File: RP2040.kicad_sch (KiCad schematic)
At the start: 23 parts, among them U1 RP2040, Y1 12MHz

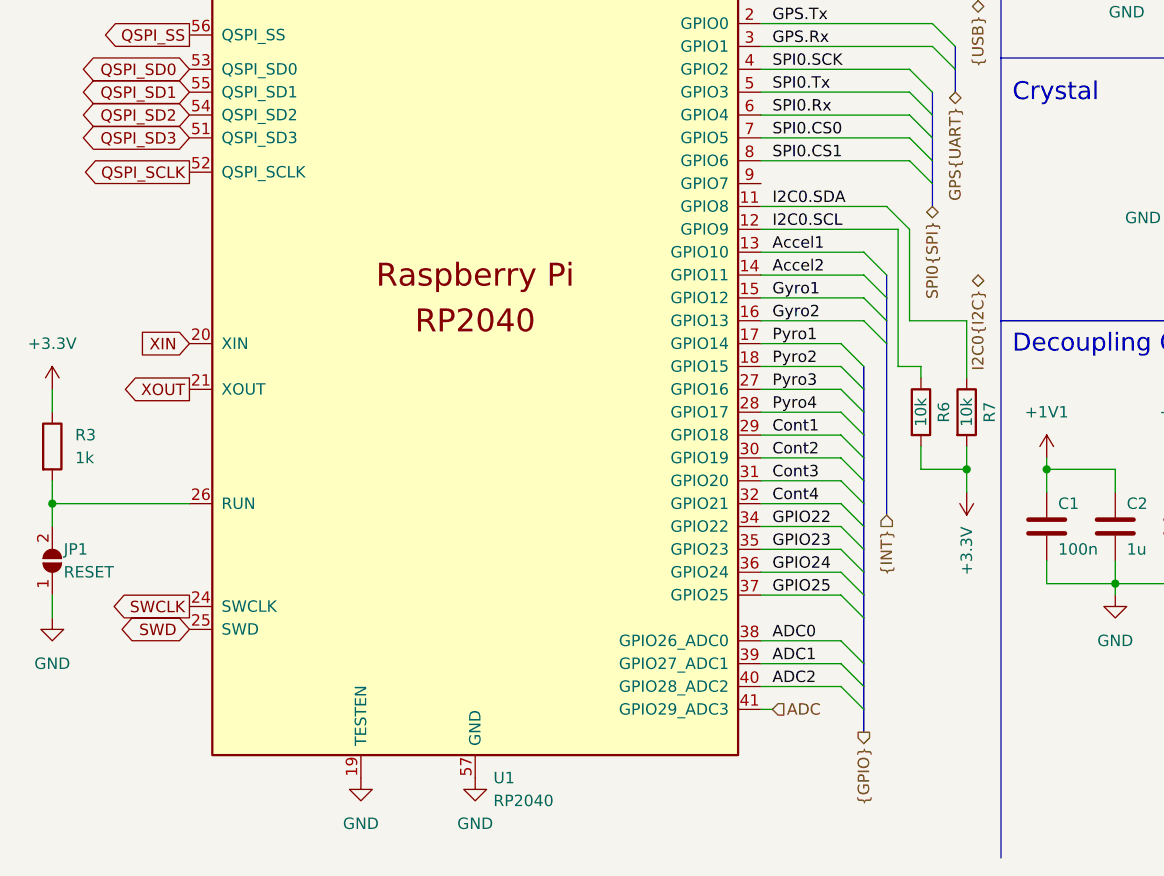
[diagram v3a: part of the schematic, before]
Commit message: Rearranged IO pins to make routing easier. Removed reset, changed BOOTSEL to button
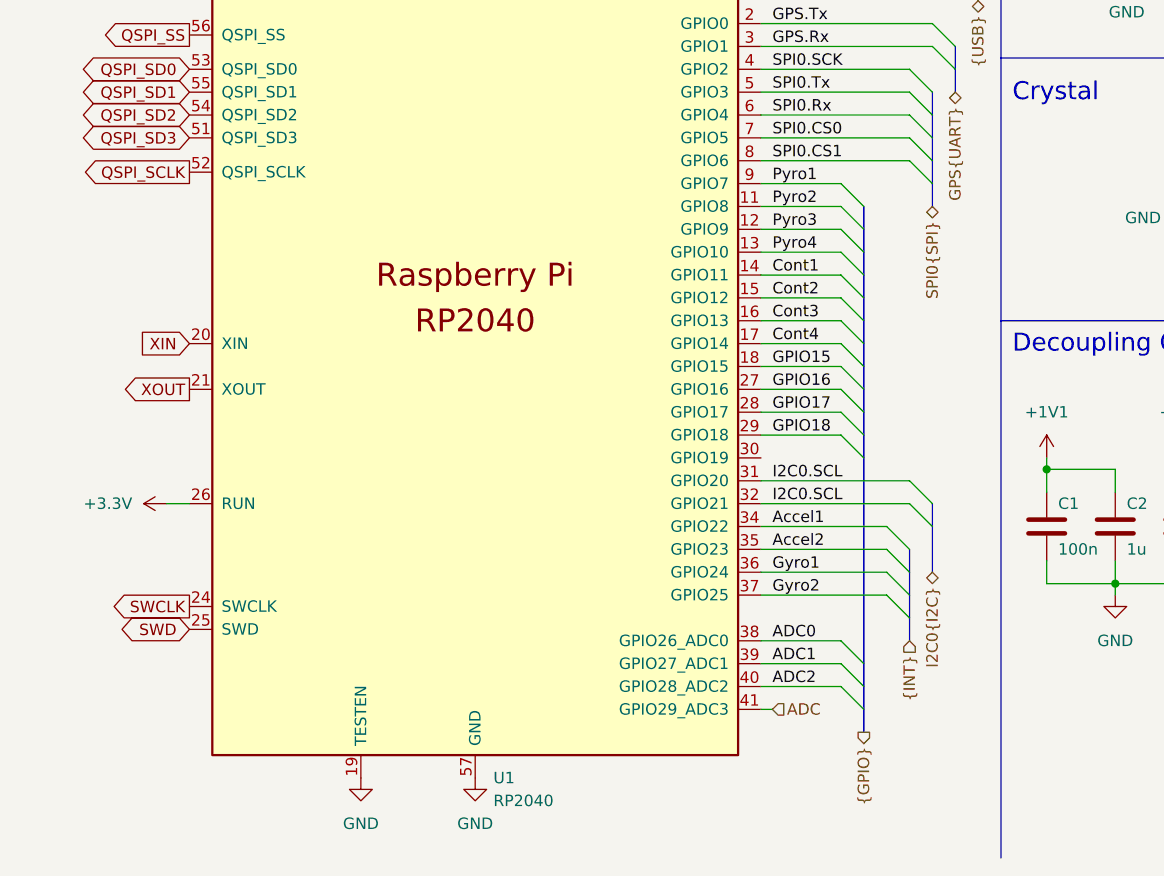
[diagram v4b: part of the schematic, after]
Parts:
- removed JP1: RESET, Jumper:SolderJumper-2_P1.3mm_Open_RoundedPad1.0x1.5mm, symbol Jumper:SolderJumper_2_Open
- removed R3: 1k, Resistor_SMD:R_0603_1608Metric, symbol Device:R
- removed R6, R7: 10k, Resistor_SMD:R_0603_1608Metric, symbol Device:R
- JP2: footprint Jumper:SolderJumper-2_P1.3mm_Open_RoundedPad1.0x1.5mm -> Button_Switch_SMD:SW_SPST_B3U-1000P
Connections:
- net GPIO22 is gone; now on net Accel1: U1.34 (GPIO22)
- net GPIO23 is gone; now on net Accel2: U1.35 (GPIO23)
- net GPIO24 is gone; now on net Gyro1: U1.36 (GPIO24)
- net GPIO25 is gone; now on net Gyro2: U1.37 (GPIO25)
- net I2C0.SDA is gone; now on net Pyro2: U1.11 (GPIO8)
- net +3V3: now also U1.26 (RUN)
- net Accel1: no longer U1.13 (GPIO10)
- net Accel2: no longer U1.14 (GPIO11)
- net Cont1: now also U1.14 (GPIO11); no longer U1.29 (GPIO18)
- net Cont2: now also U1.15 (GPIO12); no longer U1.30 (GPIO19)
- net Cont3: now also U1.16 (GPIO13); no longer U1.31 (GPIO20)
- net Cont4: now also U1.17 (GPIO14); no longer U1.32 (GPIO21)
- net Gyro1: no longer U1.15 (GPIO12)
- net Gyro2: no longer U1.16 (GPIO13)
- net I2C0.SCL: now also U1.31 (GPIO20), U1.32 (GPIO21); no longer U1.12 (GPIO9)
- net Pyro1: now also U1.9 (GPIO7); no longer U1.17 (GPIO14)
- net Pyro2: no longer U1.18 (GPIO15)
- net Pyro3: now also U1.12 (GPIO9); no longer U1.27 (GPIO16)
- net Pyro4: now also U1.13 (GPIO10); no longer U1.28 (GPIO17)
- new net GPIO15: U1.18 (GPIO15)
- new net GPIO16: U1.27 (GPIO16)
- new net GPIO17: U1.28 (GPIO17)
- new net GPIO18: U1.29 (GPIO18)

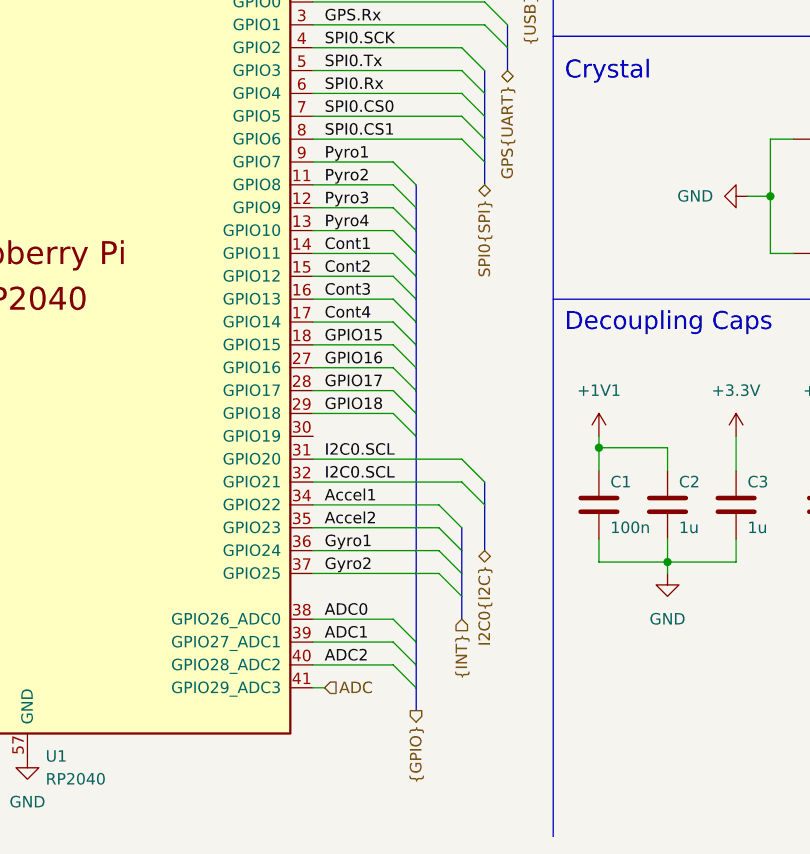
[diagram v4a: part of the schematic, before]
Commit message: Removed GPIO, changed footprints
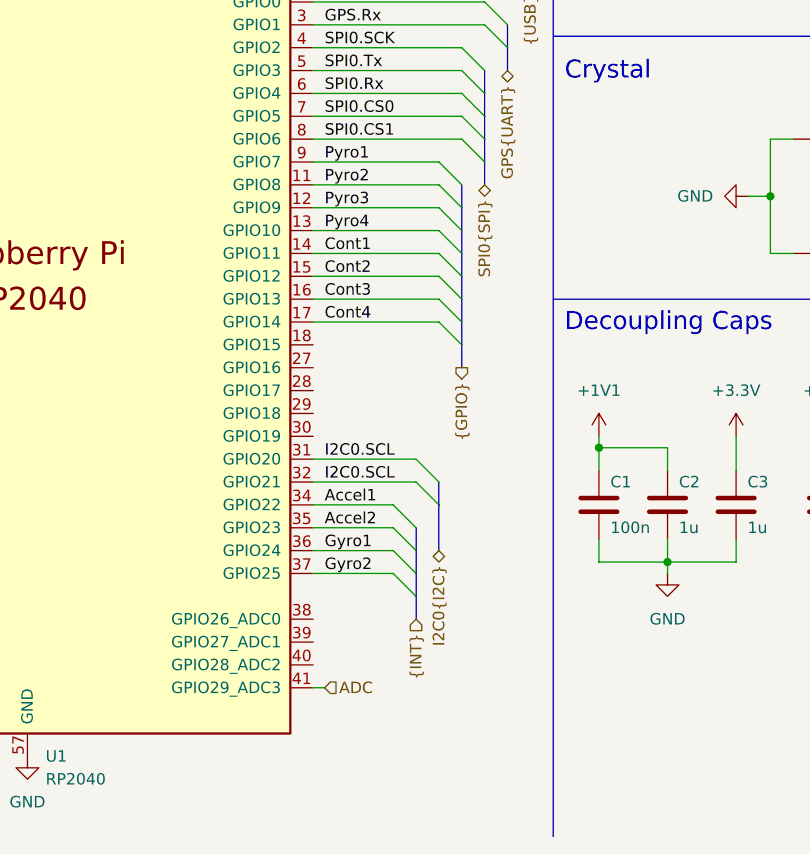
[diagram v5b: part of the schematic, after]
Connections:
- net ADC0: no longer names the net of U1.38 (GPIO26_ADC0)
- net ADC1: no longer names the net of U1.39 (GPIO27_ADC1)
- net ADC2: no longer names the net of U1.40 (GPIO28_ADC2)
- net GPIO15: no longer names the net of U1.18 (GPIO15)
- net GPIO16: no longer names the net of U1.27 (GPIO16)
- net GPIO17: no longer names the net of U1.28 (GPIO17)
- net GPIO18: no longer names the net of U1.29 (GPIO18)

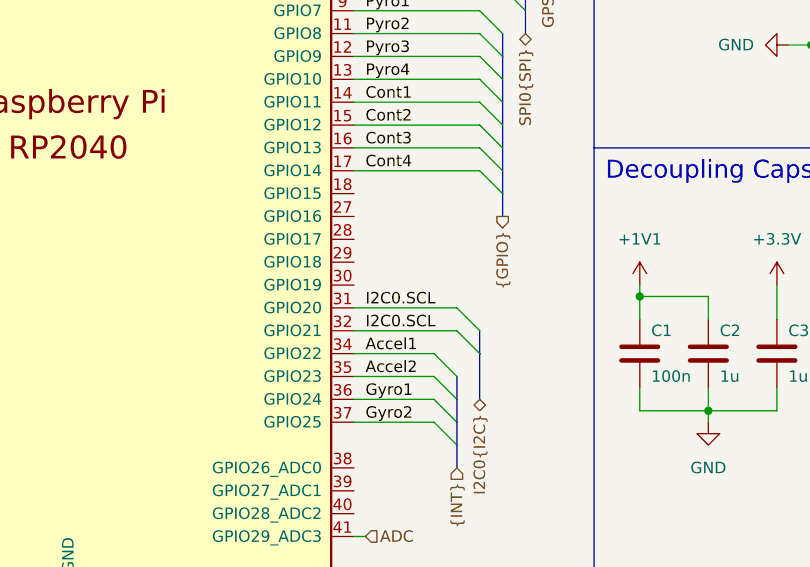
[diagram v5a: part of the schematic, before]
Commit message: Rearrange parts of PCB
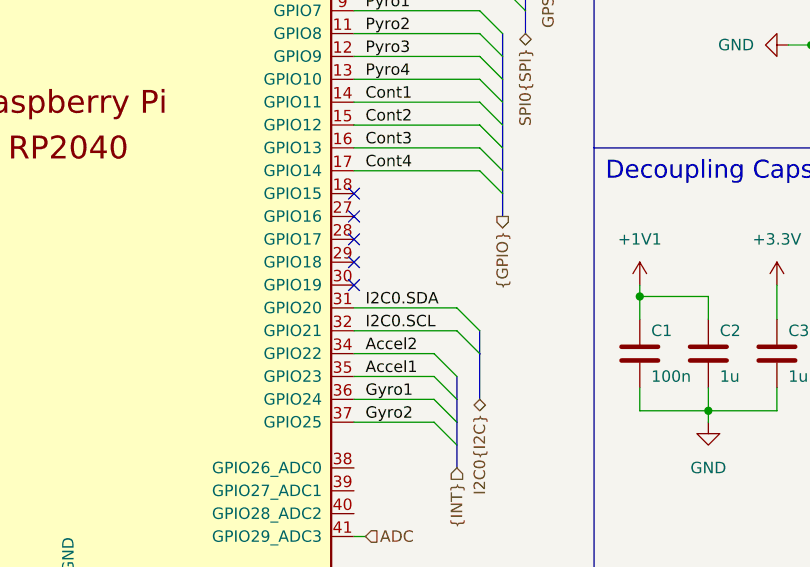
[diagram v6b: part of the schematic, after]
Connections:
- net Accel1: now also U1.35 (GPIO23); no longer U1.34 (GPIO22)
- net Accel2: now also U1.34 (GPIO22); no longer U1.35 (GPIO23)
- net I2C0.SCL: no longer U1.31 (GPIO20)
- new net I2C0.SDA: U1.31 (GPIO20)
- no-connect marks 0 -> 5
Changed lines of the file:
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@@
   (junction (at 46.99 22.86) (diameter 0) (color 0 0 0 0)
   )
+  (no_connect (at 95.25 91.44))
+  (no_connect (at 95.25 81.28))
+  (no_connect (at 95.25 83.82))
+  (no_connect (at 95.25 88.9))
+  (no_connect (at 95.25 86.36))
   (bus_entry (at 114.3 58.42) (size -2.54 -2.54)
     (stroke (width 0) (type default) (color 0 0 0 0))
@@
     (effects (font (size 1.27 1.27)) (justify left bottom))
   )
-  (label "Accel1" (at 96.52 99.06 0)
+  (label "Accel2" (at 96.52 99.06 0)
     (effects (font (size 1.27 1.27)) (justify left bottom))
   )
@@
     (effects (font (size 1.27 1.27)) (justify left bottom))
   )
-  (label "I2C0.SCL" (at 96.52 93.98 0)
+  (label "I2C0.SDA" (at 96.52 93.98 0)
     (effects (font (size 1.27 1.27)) (justify left bottom))
   )
@@
     (effects (font (size 1.27 1.27)) (justify left bottom))
   )
-  (label "Accel2" (at 96.52 101.6 0)
-    (effects (font (size 1.27 1.27)) (justify left bottom))
-  )
+  (label "Accel1" (at 96.52 101.6 0)
+    (effects (font (size 1.27 1.27)) (justify left bottom))
+  )

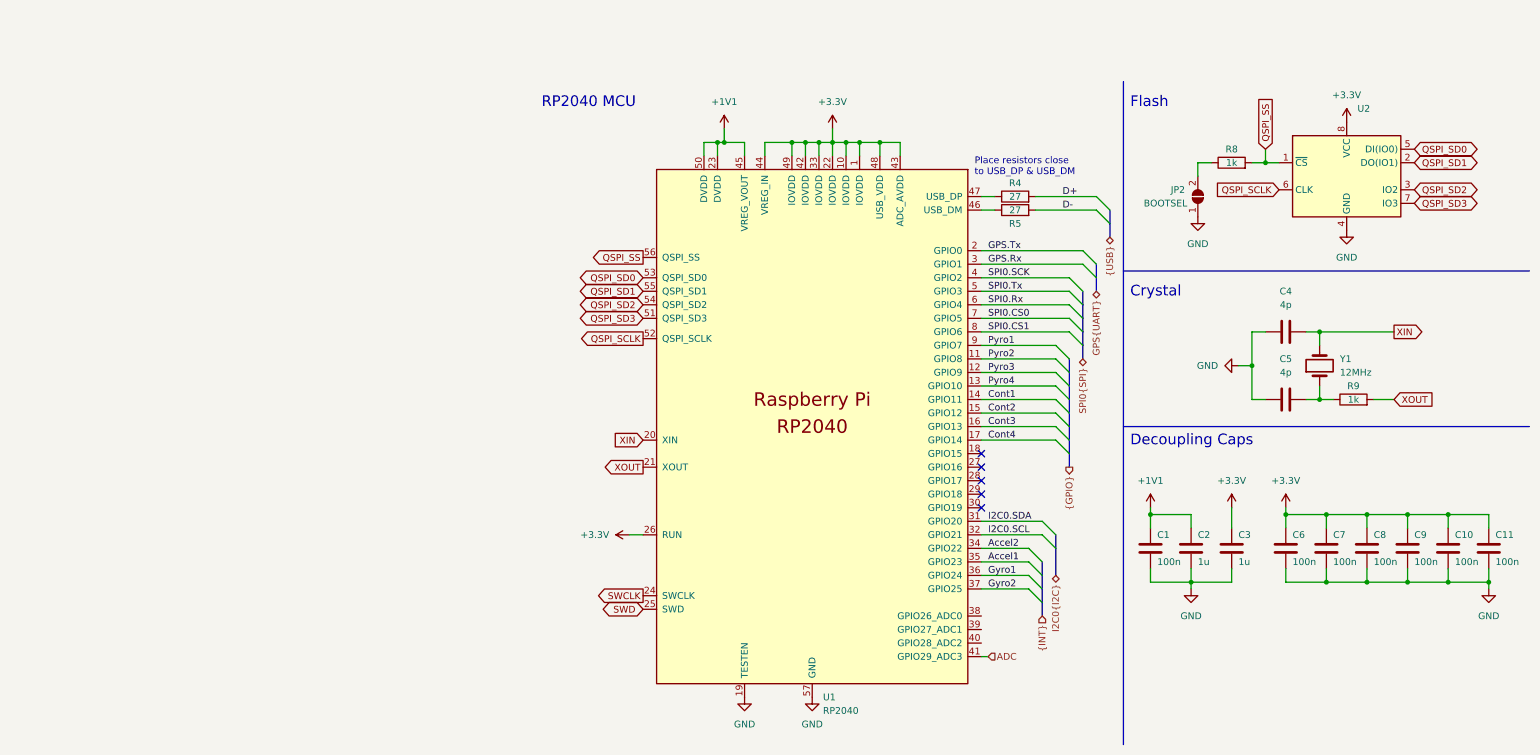
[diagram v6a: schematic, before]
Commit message: Routed pyros. Placed decoupling capacitors
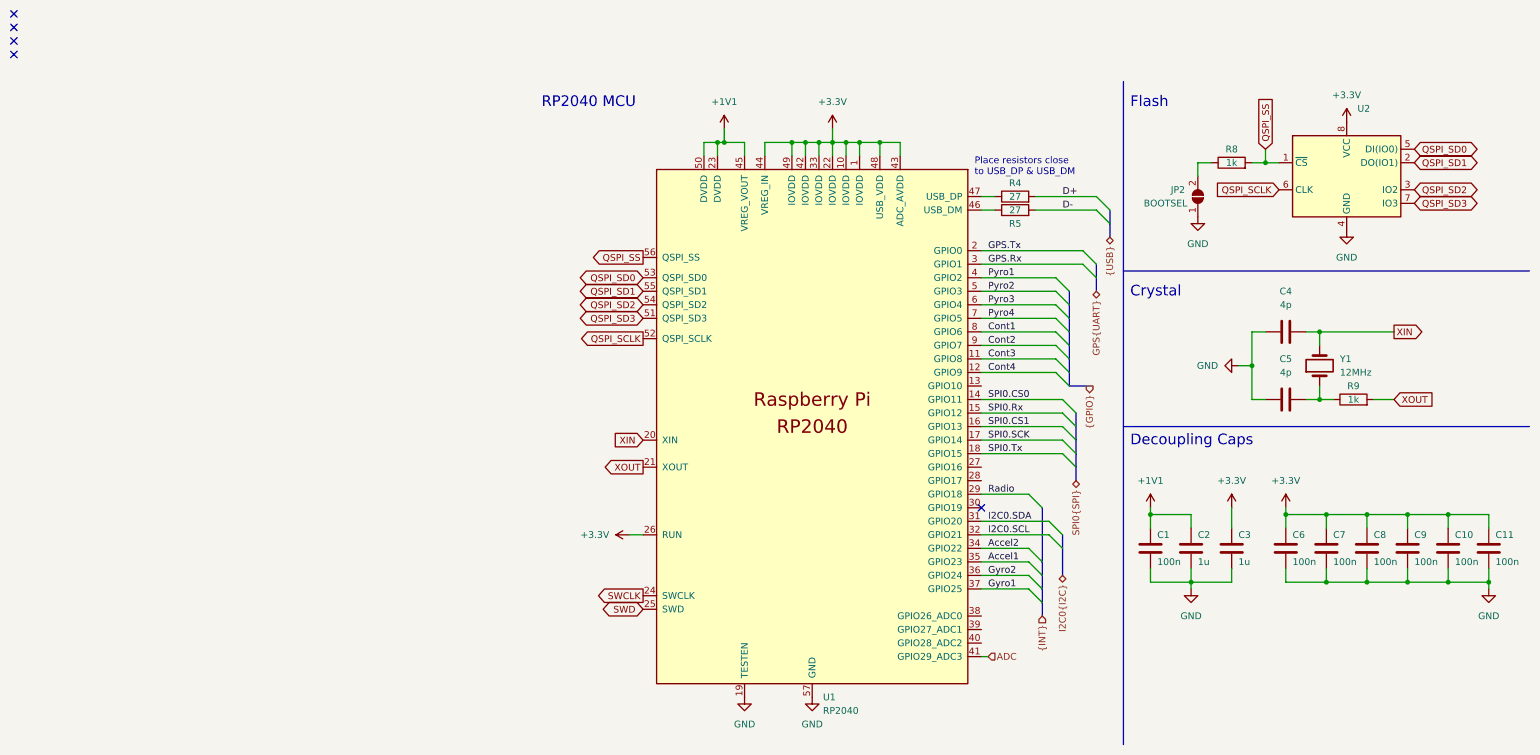
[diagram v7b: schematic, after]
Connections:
- net Cont1: now also U1.8 (GPIO6); no longer U1.14 (GPIO11)
- net Cont2: now also U1.9 (GPIO7); no longer U1.15 (GPIO12)
- net Cont3: now also U1.11 (GPIO8); no longer U1.16 (GPIO13)
- net Cont4: now also U1.12 (GPIO9); no longer U1.17 (GPIO14)
- net Gyro1: now also U1.37 (GPIO25); no longer U1.36 (GPIO24)
- net Gyro2: now also U1.36 (GPIO24); no longer U1.37 (GPIO25)
- net Pyro1: now also U1.4 (GPIO2); no longer U1.9 (GPIO7)
- net Pyro2: now also U1.5 (GPIO3); no longer U1.11 (GPIO8)
- net Pyro3: now also U1.6 (GPIO4); no longer U1.12 (GPIO9)
- net Pyro4: now also U1.7 (GPIO5); no longer U1.13 (GPIO10)
- net SPI0.CS0: now also U1.14 (GPIO11); no longer U1.7 (GPIO5)
- net SPI0.CS1: now also U1.16 (GPIO13); no longer U1.8 (GPIO6)
- net SPI0.Rx: now also U1.15 (GPIO12); no longer U1.6 (GPIO4)
- net SPI0.SCK: now also U1.17 (GPIO14); no longer U1.4 (GPIO2)
- net SPI0.Tx: now also U1.18 (GPIO15); no longer U1.5 (GPIO3)
- net Radio: now reaches U1.29 (GPIO18)
